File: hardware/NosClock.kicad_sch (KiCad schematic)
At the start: 32 parts, among them J101 USB_C_Receptacle_USB2.0_16P, J102 Conn_01x02, J103 Conn_01x04, J104 12V IN, U101 ESP32-C3-MINI-1, U103 DS3231MZ

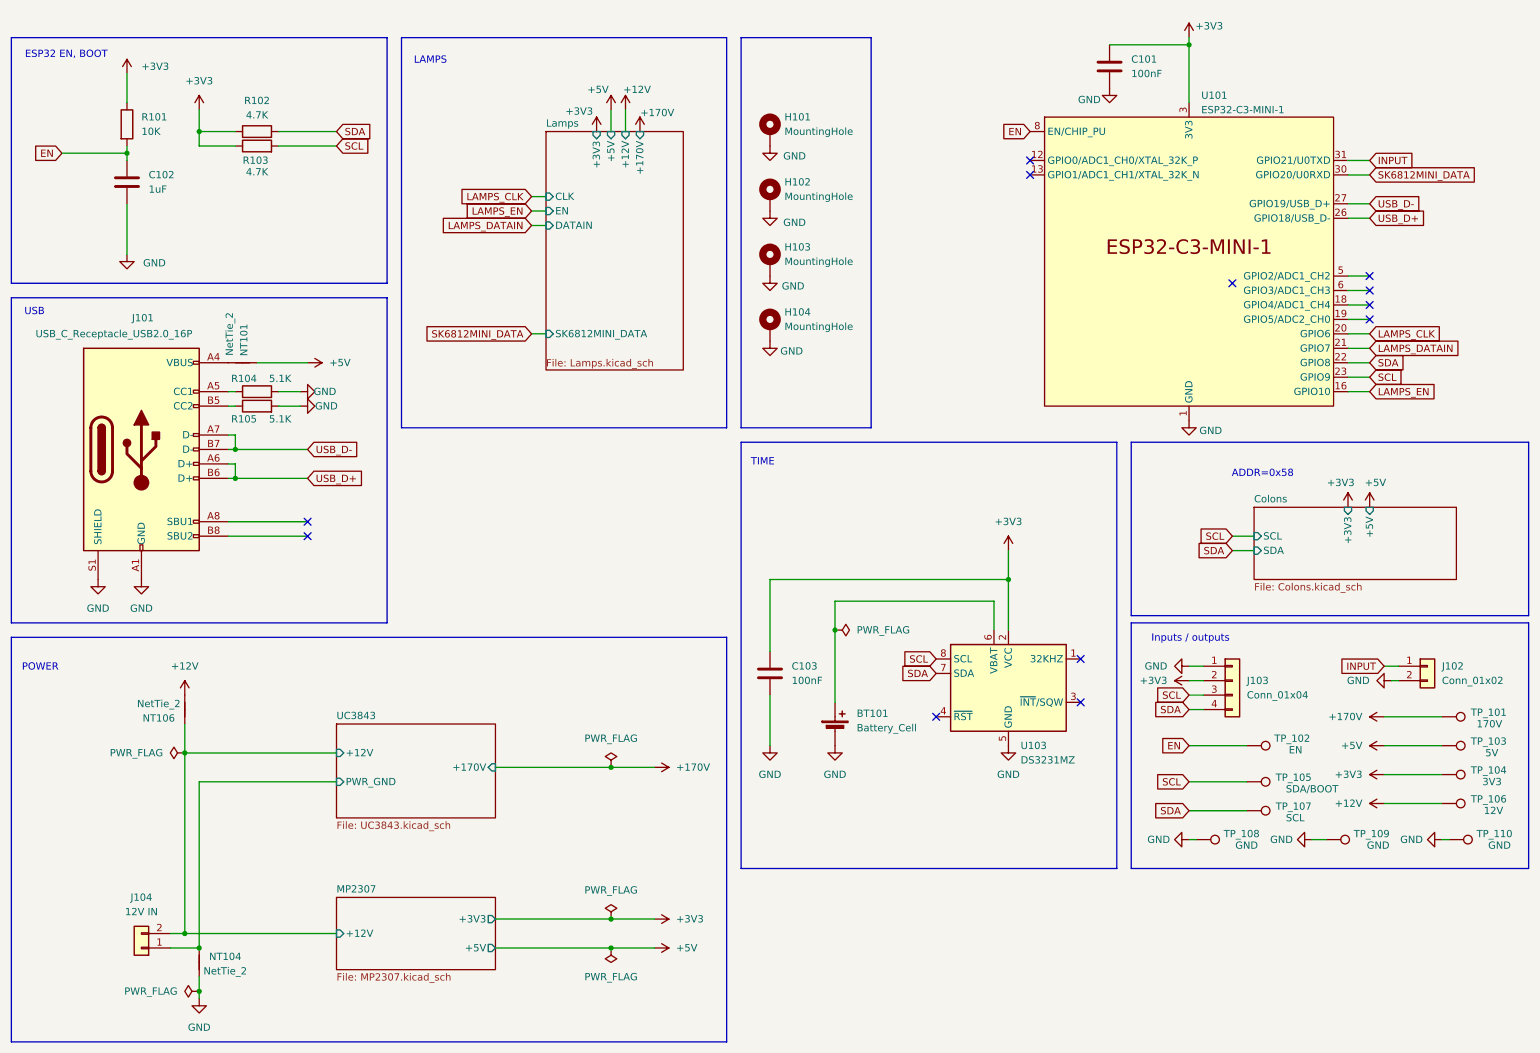
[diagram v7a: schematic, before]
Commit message: bugfixing
- usb- and usb+ messed up
- wrong boot label
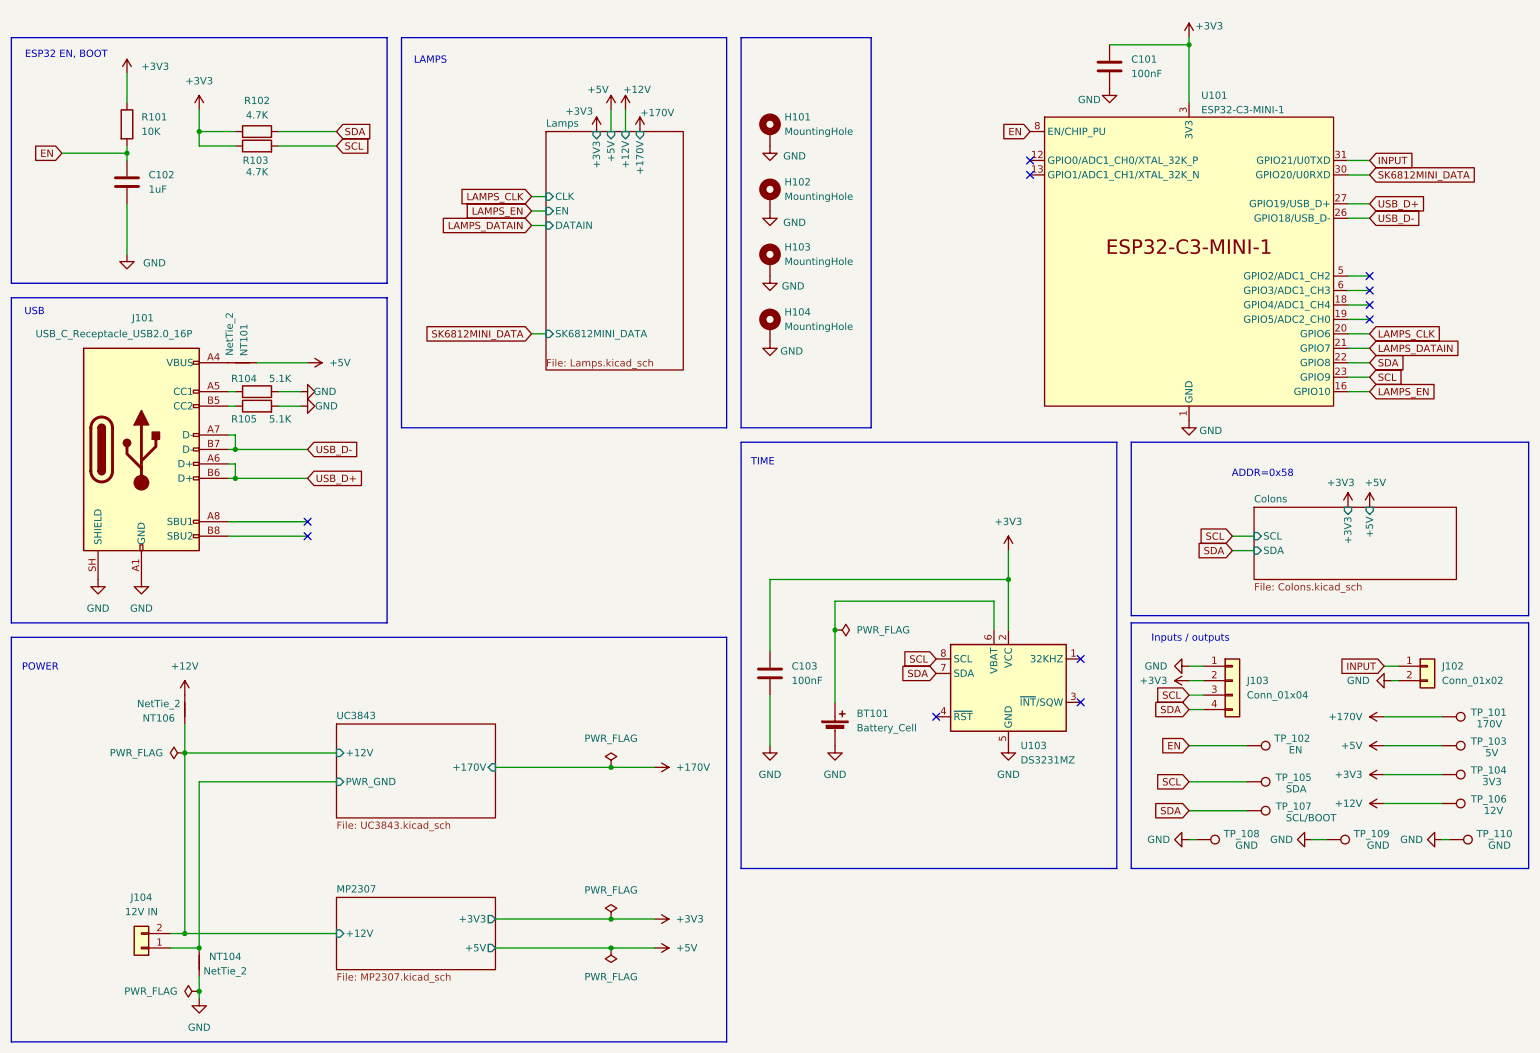
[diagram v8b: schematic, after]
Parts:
- TP_105: value SDA/BOOT -> SDA
- TP_107: value SCL -> SCL/BOOT
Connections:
- net GND: now also J101.SH (SHIELD); no longer J101.S1 (SHIELD)
- net USB_D+: now also U101.27 (GPIO19/USB_D+); no longer U101.26 (GPIO18/USB_D-)
- net USB_D-: now also U101.26 (GPIO18/USB_D-); no longer U101.27 (GPIO19/USB_D+)
- no-connect marks 12 -> 11
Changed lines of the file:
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@@
 	)
 	(no_connect
-		(at 231.14 59.69)
-	)
-	(no_connect
 		(at 68.58 104.14)
 	)
@@
 	(global_label "USB_D+"
 		(shape input)
-		(at 255.27 48.26 0)
+		(at 255.27 45.72 0)
 		(fields_autoplaced yes)
 		(effects
@@
 		)
 		(property "Intersheetrefs" "${INTERSHEET_REFS}"
-			(at 265.8752 48.26 0)
+			(at 265.8752 45.72 0)
 			(hide yes)
 			(show_name no)
@@
 		)
 	)
-	(global_label "USB_D-"
+	(global_label "SCL"
 		(shape input)
-		(at 255.27 45.72 0)
+		(at 231.14 104.14 180)
 		(fields_autoplaced yes)
 		(effects
@@
 				(size 1.27 1.27)
 			)
-			(justify left)
+			(justify right)
 		)
 		(property "Intersheetrefs" "${INTERSHEET_REFS}"
-			(at 265.8752 45.72 0)
+			(at 224.6472 104.14 0)
 			(hide yes)
 			(show_name no)
@@
 					(size 1.27 1.27)
 				)
-				(justify left)
+				(justify right)
 			)
 		)
 	)
-	(global_label "SCL"
+	(global_label "USB_D-"
 		(shape input)
-		(at 231.14 104.14 180)
+		(at 255.27 48.26 0)
 		(fields_autoplaced yes)
 		(effects
@@
 				(size 1.27 1.27)
 			)
-			(justify right)
+			(justify left)
 		)
 		(property "Intersheetrefs" "${INTERSHEET_REFS}"
-			(at 224.6472 104.14 0)
+			(at 265.8752 48.26 0)
 			(hide yes)
 			(show_name no)
@@
 					(size 1.27 1.27)
 				)
-				(justify right)
+				(justify left)
 			)
 		)
@@
 			)
 		)
-		(pin "S1"
+		(pin "SH"
 		)
 		(pin "B5"
@@
 			)
 		)
-		(property "Value" "SDA/BOOT"
+		(property "Value" "SDA"
 			(at 240.538 148.59 90)
 			(show_name no)
@@
 			)
 		)
-		(property "Value" "SCL"
+		(property "Value" "SCL/BOOT"
 			(at 240.538 153.67 90)
 			(show_name no)
